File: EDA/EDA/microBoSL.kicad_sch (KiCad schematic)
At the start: 57 parts

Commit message: rebase for adding wireless to microbosl
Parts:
- removed C12, C13, C14, C2, C3, C4, C7: (no value), symbol Device:C
- removed D4: (no value), symbol Device:D
- removed J10, J9: (no value), symbol Connector_Generic:Conn_01x02
- removed J11, J12, J13, J2, J5: (no value), symbol Connector_Generic:Conn_01x03
- removed J6: (no value), symbol Connector_Generic:Conn_01x04
- removed Q1, Q2: (no value), symbol microBoSL-rescue:DMP2165UW
- removed R1, R11, R12, R5, R6: (no value), symbol Device:R
- removed SW2: (no value), symbol microBoSL-rescue:AYZ0103AGRLC
- removed U10: (no value), symbol microBoSL-rescue:TPS709A33DBVT
- removed U3: (no value), Package_DFN_QFN:QFN-28-1EP_4x4mm_P0.45mm_EP2.4x2.4mm, symbol MCU_Microchip_ATmega:ATmega328P-MM
- removed U4, U8, U9: (no value), symbol Driver_Motor:ZXBM5210-S
- removed U?: (no value), symbol Timer_RTC:MCP7940N-xSN
- added J2: (no value), symbol Connector_Generic:Conn_02x03_Odd_Even
- added J3: (no value), symbol Connector_Generic:Conn_01x04
- added J6: (no value), symbol Connector_Generic:Conn_01x10
- added Q1: (no value), symbol Device:Q_NMOS_GSD
- added R2: (no value), symbol Device:R
- added U1, U2: (no value), symbol Analog_Switch:MAX40200ANS
- added U3: (no value), symbol Regulator_Linear:MCP1700-3302E_SOT23
- added U4: (no value), symbol microBoSL-rescue:ATmega328-MMH-MCU_Microchip_ATmega
- added U5: (no value), symbol microBoSL-rescue:MCP7940N-xSN-Timer
- C1: Supplier https://au.mouser.com/ProductDetail/Samsung-Electro-Mechani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 -> (none)
- C2: renamed from C6; Supplier https://au.mouser.com/ProductDetail/KEMET/C0402C150J8HACTU?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 -> (none)
- C3: renamed from C5; Supplier https://au.mouser.com/ProductDetail/KEMET/C0402C150J8HACTU?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 -> (none)
- C4: renamed from C9; Supplier https://au.mouser.com/ProductDetail/KEMET/C0402C150J8HACTU?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 -> (none)
- C5: renamed from C8; Supplier https://au.mouser.com/ProductDetail/KEMET/C0402C150J8HACTU?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 -> (none)
- C6: renamed from C10; Supplier https://au.mouser.com/ProductDetail/AVX/04026D104KAT2A?qs=s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 -> (none)
- C7: renamed from C11; Supplier https://au.mouser.com/ProductDetail/AVX/04026D104KAT2A?qs=s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 -> (none)
- D1: renamed from D2; Supplier https://au.mouser.com/ProductDetail/Wurth-Elektronik/150060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 -> (none)
- D2: renamed from D3; Supplier https://au.mouser.com/datasheet/2/445/150060YS55040-1714218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 -> (none)
- D3: renamed from D1; Supplier https://au.mouser.com/ProductDetail/Wurth-Elektronik/150060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 -> (none)
- J8: Supplier https://au.mouser.com/ProductDetail/Molex/105133-0001?qs=nm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 -> (none)
- R1: renamed from R2; Supplier https://au.mouser.com/ProductDetail/Vishay-Dale/CRCW040210K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 -> (none)
- R3: renamed from R4; Supplier https://au.mouser.com/ProductDetail/Vishay-Dale/CRCW040210K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 -> (none)
- R4: renamed from R3; Supplier https://au.mouser.com/ProductDetail/Vishay-Dale/CRCW040210K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 -> (none)
- R5: renamed from R7; Supplier https://au.mouser.com/ProductDetail/Vishay-Dale/CRCW040210K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 -> (none)
- R6: renamed from R8; Supplier https://au.mouser.com/ProductDetail/Vishay-Dale/CRCW04023K3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 -> (none)
- R7: renamed from R9; Supplier https://au.mouser.com/ProductDetail/Vishay-Dale/CRCW04023K3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 -> (none)
- R8: renamed from R10; Supplier https://au.mouser.com/ProductDetail/Vishay-Dale/CRCW04023K3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 -> (none)
- U6: renamed from U5; Supplier https://au.mouser.com/ProductDetail/Nexperia/74HC126PW-Q100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 -> (none)
- U7: Supplier https://au.mouser.com/ProductDetail/FTDI/FT232RQ-REEL?qs=D1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 -> (none)
- Y1: Supplier https://au.mouser.com/ProductDetail/Diodes-Incorporated/F90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 -> (none)
- Y2: Supplier https://au.mouser.com/ProductDetail/IQD/LFXTAL050789Reel?qs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 -> (none)
- renumbered J3 to J4, J4 to J5
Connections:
- net VBAT is gone; now on net VPP: J4.2 (Pin_2)
- net AREF: now also U4.17 (AREF)
- net GND: now also J7.2 (Pin_2), J2.1 (Pin_1), J2.2 (Pin_2), J3.1 (Pin_1), Q1.2 (S), R2.1, U1.B2 (GND), U2.B2 (GND), U3.1 (GND), U4.18 (GND), U4.29 (GND), U4.4 (GND), U5.3 (VBAT), U5.4 (VSS)
- net Hall_WKE_S: now also J2.5 (Pin_5), U4.21 (PC2)
- net RTC_I: now also U4.28 (PD2), U5.7 (MFP)
- net SCL: now also U4.24 (PC5), U5.6 (SCL)
- net SDA: now also U4.23 (PC4), U5.5 (SDA)
- net TLL_RST: now also J3.2 (Pin_2), U4.25 (~{RESET}/PC6)
- net TLL_RX: now also J3.3 (Pin_3), U4.26 (PD0)
- net TLL_TX: now also J3.4 (Pin_4), U4.27 (PD1)
- net USB_V: now also U1.A1 (VDD), U1.B1 (EN)
- net VPP: now also U2.A1 (VDD), U2.B1 (EN)
- net V_3.3: now also U3.2 (VO), U4.16 (AVCC), U4.3 (VCC), U5.8 (VCC)
- net at C2.2, Y1.1: now also U4.6 (XTAL2/PB7)
- net at C3.2, Y1.3: now also U4.5 (XTAL1/PB6)
- net at C4.2, Y2.1: now also U5.1 (X1)
- net at C5.2, Y2.2: now also U5.2 (X2)
- net at J7.1 (Pin_1): now also Q1.3 (D)
- new net: U1.A2 (OUT), U2.A2 (OUT), U3.3 (VI)
- new net A1: J6.9 (Pin_9), U4.20 (PC1)
- new net A3: J6.10 (Pin_10), U4.22 (PC3)
- new net D10: J6.5 (Pin_5), U4.12 (PB2)
- new net D11: J6.6 (Pin_6), U4.13 (PB3)
- new net D12: J6.7 (Pin_7), U4.14 (PB4)
- new net D13: J6.8 (Pin_8), U4.15 (PB5)
- new net D3: J6.1 (Pin_1), U4.1 (PD3)
- new net D4: J6.2 (Pin_2), U4.2 (PD4)
- new net D7: J6.3 (Pin_3), U4.9 (PD7)
- new net D8: J6.4 (Pin_4), U4.10 (PB0)
- new net Hall_CNT_P: J2.4 (Pin_4), U4.8 (PD6)
- new net Hall_CNT_S: J2.6 (Pin_6), U4.19 (PC0)
- new net Hall_WKE_P: J2.3 (Pin_3), U4.7 (PD5)
- new net MOSFET: Q1.1 (G), R2.2, U4.11 (PB1)
- no-connect marks 18 -> 15
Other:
- note added: "Hall Count"
- note added: "Motor MOSFET"
- note removed: "Battery Switch"
- note removed: "Motor H Bridges"
- moved on the sheet: C2, C3, C4, C5, C6, C7, D1, D2, D3, J1, J4, J5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

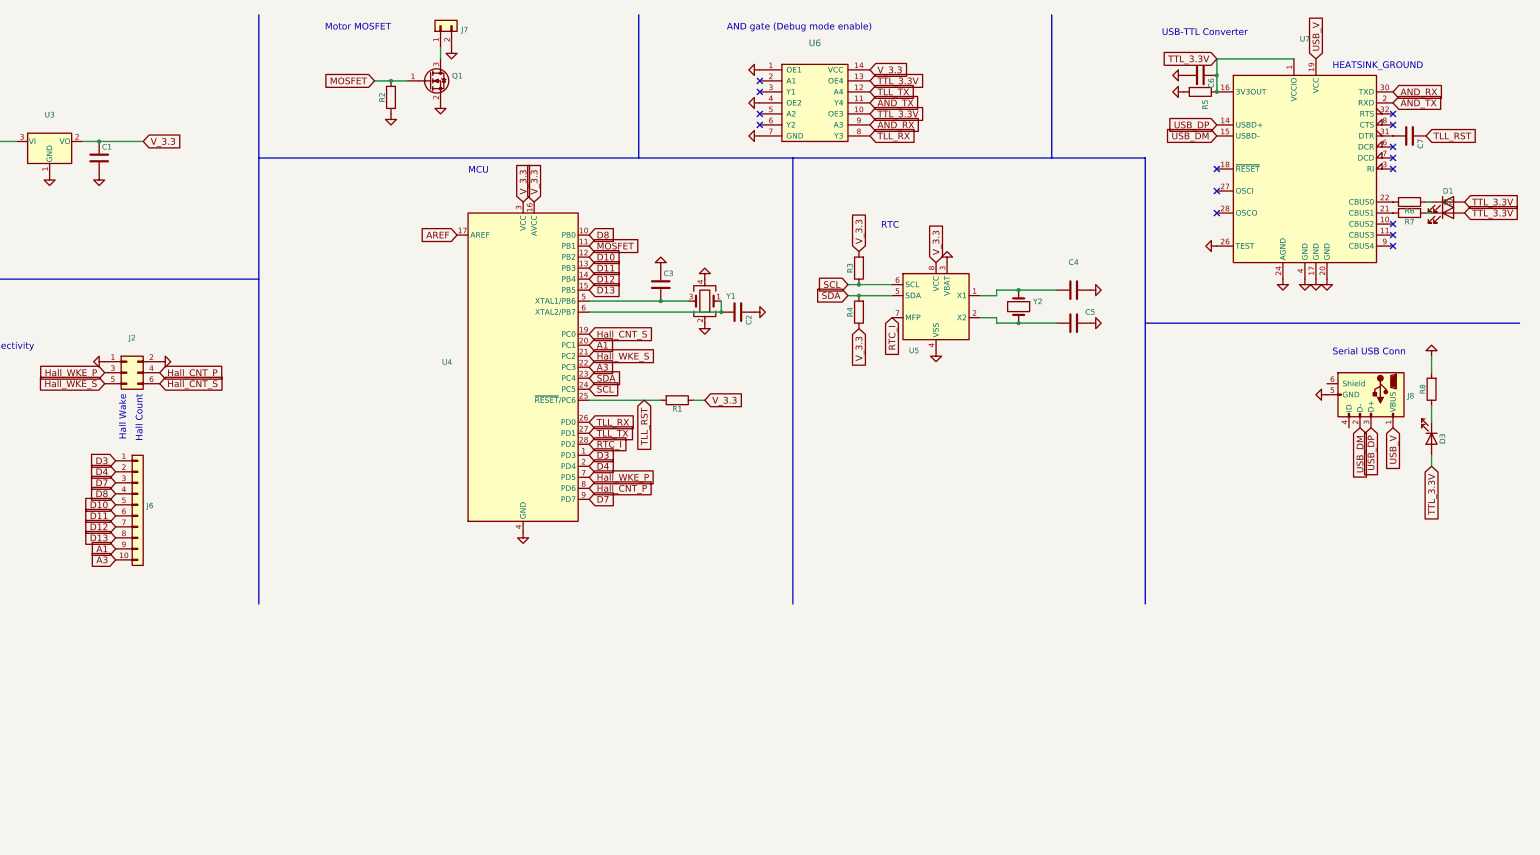
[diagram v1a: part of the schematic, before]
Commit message: added Si4463 radio module
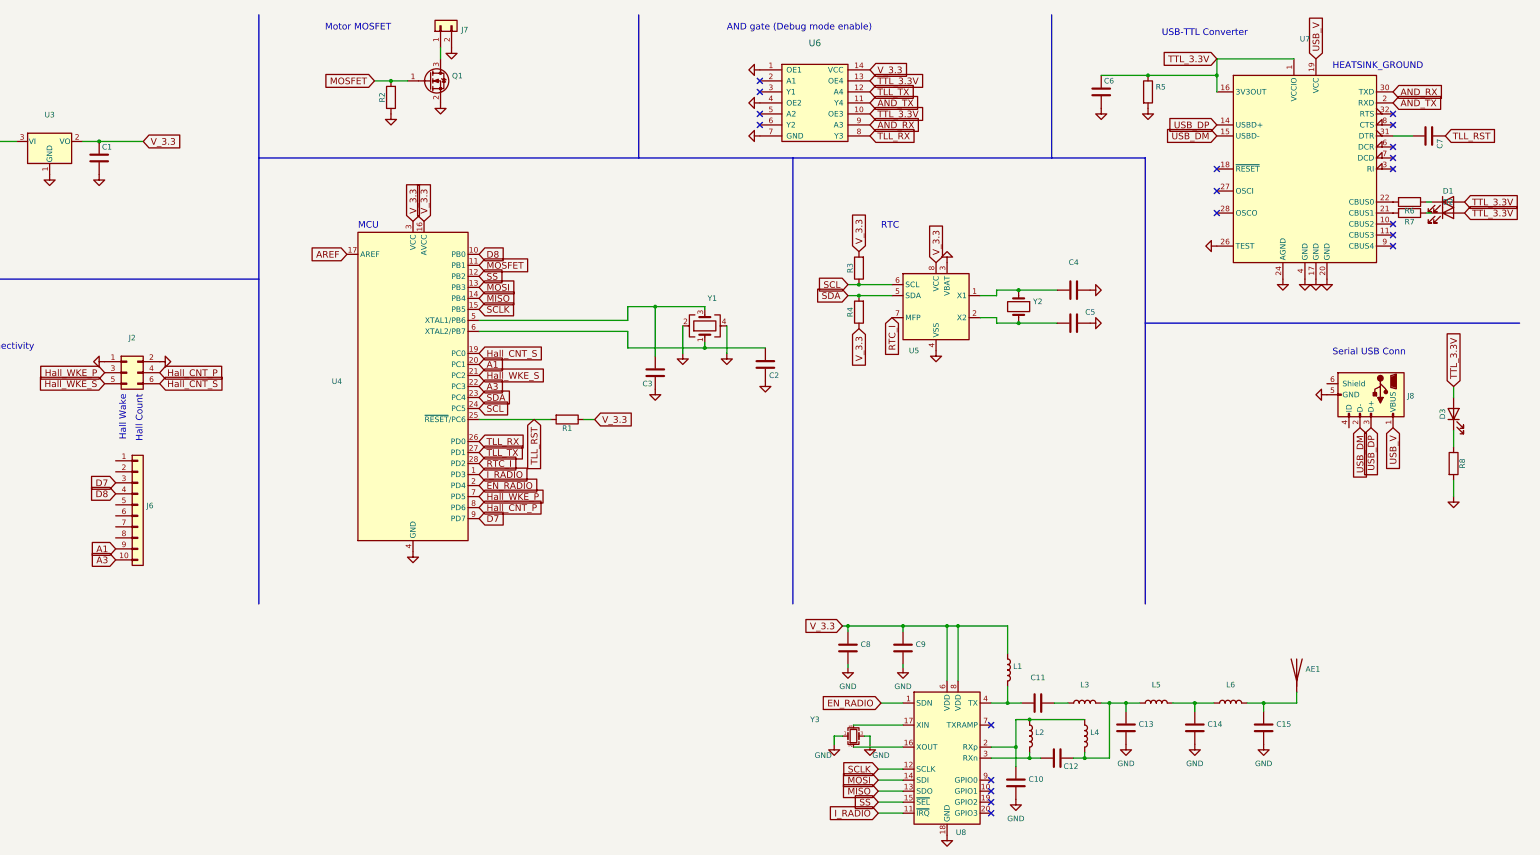
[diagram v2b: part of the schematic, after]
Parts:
- added AE1: (no value), symbol Device:Antenna
- added C10, C12, C13, C14, C15: (no value), Capacitor_SMD:C_0402_1005Metric, symbol Device:C
- added C11, C8, C9: (no value), symbol Device:C
- added L1, L2: (no value), symbol Device:L
- added L3, L4, L5, L6: (no value), Inductor_SMD:L_0402_1005Metric, symbol Device:L
- added U8: (no value), symbol RF:Si4463
- added Y3: (no value), symbol Device:Crystal_GND24_Small
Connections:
- net GND: now also C10.2, C13.2, C14.2, C15.2, C8.2, C9.2, U8.18 (GND), U8.21 (GND), Y3.1, Y3.3
- net V_3.3: now also C8.1, C9.1, L1.1, U8.6 (VDD), U8.8 (VDD)
- net D10: no longer names the net of J6.5 (Pin_5)
- net D10: no longer U4.12 (PB2)
- net D11: no longer names the net of J6.6 (Pin_6)
- net D11: no longer U4.13 (PB3)
- net D12: no longer names the net of J6.7 (Pin_7)
- net D12: no longer U4.14 (PB4)
- net D13: no longer names the net of J6.8 (Pin_8)
- net D13: no longer U4.15 (PB5)
- net D3: no longer names the net of J6.1 (Pin_1)
- net D3: no longer U4.1 (PD3)
- net D4: no longer names the net of J6.2 (Pin_2)
- net D4: no longer U4.2 (PD4)
- new net: C12.1, C13.1, L3.2, L4.2, L5.1
- new net: C14.1, L5.2, L6.1
- new net: C11.1, L3.1
- new net: C11.2, L1.2, U8.4 (TX)
- new net: C10.1, L2.1, L4.1, U8.2 (RXp)
- new net: C12.2, L2.2, U8.3 (RXn)
- new net: AE1.1 (A), C15.1, L6.2
- new net: U8.16 (XOUT), Y3.2
- new net: U8.17 (XIN), Y3.4
- new net EN_RADIO: U4.2 (PD4), U8.1 (SDN)
- new net I_RADIO: U4.1 (PD3), U8.11 (~{IRQ})
- new net MISO: U4.14 (PB4), U8.13 (SDO)
- new net MOSI: U4.13 (PB3), U8.14 (SDI)
- new net SCLK: U4.15 (PB5), U8.12 (SCLK)
- new net SS: U4.12 (PB2), U8.15 (~{SEL})
- no-connect marks 15 -> 20
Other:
- moved on the sheet: C2, C3, C6, C7, D3, R1, R5, R8, U4, Y1

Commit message: finalised schematic for radio microbosl
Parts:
- removed J2: (no value), symbol Connector_Generic:Conn_02x03_Odd_Even
- removed J6: (no value), symbol Connector_Generic:Conn_01x10
- removed J7: (no value), symbol Connector_Generic:Conn_01x02
- removed Q1: (no value), symbol Device:Q_NMOS_GSD
- removed U1, U2: (no value), symbol Analog_Switch:MAX40200ANS
- removed U3: (no value), symbol Regulator_Linear:MCP1700-3302E_SOT23
- removed U5: (no value), symbol microBoSL-rescue:MCP7940N-xSN-Timer
- added C16: 100 nF, Capacitor_SMD:C_0402_1005Metric, symbol Device:C
- added C17, C18: 15 pF, Capacitor_SMD:C_0402_1005Metric, symbol Device:C
- added D4: CUS08F30,H3F, Diode_SMD:D_SOD-323, symbol Device:D
- added F1: (no value), symbol Device:Fuse_Small
- added J2: Conn_01x03, Connector_PinHeader_2.54mm:PinHeader_1x03_P2.54mm_Vertical, symbol Connector_Generic:Conn_01x03
- added J6, J7: (no value), symbol Connector_Generic:Conn_01x03
- added J9: MOTOR_OUT, Connector_PinHeader_2.54mm:PinHeader_1x02_P2.54mm_Vertical, symbol Connector_Generic:Conn_01x02
- added Q1, Q2: DMP2165UW, Package_TO_SOT_SMD:SOT-323_SC-70, symbol microBoSL-rescue:DMP2165UW
- added R10, R9: 10 kΩ, Resistor_SMD:R_0402_1005Metric, symbol Device:R
- added R11, R12: 4.7 MΩ, Capacitor_SMD:C_0402_1005Metric, symbol Device:R
- added SW2: (no value), symbol Switch:SW_SPDT
- added U1: TPS709A33DBVT, Package_TO_SOT_SMD:SOT-23-5, symbol microBoSL-rescue:TPS709A33DBVT
- added U2: ZXBM5210-S, Package_SO:SOIC-8_3.9x4.9mm_P1.27mm, symbol Driver_Motor:ZXBM5210-S
- added U3: (no value), symbol Timer_RTC:MCP7940N-xMNY
- AE1: value (none) -> Antenna; footprint (none) -> Connector_PinHeader_2.54mm:PinHeader_1x01_P2.54mm_Vertical
- C1: value (none) -> 2.2 μF; footprint (none) -> Capacitor_SMD:C_0805_2012Metric; Supplier (none) -> https://au.mouser.com/ProductDetail/Samsung-Electro-Mechani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
- C10, C12: value (none) -> 5.1 pF
- C11: value (none) -> 6.8 pF; footprint (none) -> Capacitor_SMD:C_0402_1005Metric
- C13: value (none) -> 12 pF
- C14: value (none) -> 18 pF
- C15: value (none) -> 9.1 pF
- C2, C3: value (none) -> 22 pF; footprint (none) -> Capacitor_SMD:C_0402_1005Metric
- C4, C5: value (none) -> 100 nF; footprint (none) -> Capacitor_SMD:C_0402_1005Metric; Supplier (none) -> https://au.mouser.com/ProductDetail/AVX/04026D104KAT2A?qs=s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
- C6, C7: value (none) -> 100 nF; footprint (none) -> Capacitor_SMD:C_0603_1608Metric
- C8: value (none) -> 100 pF; footprint (none) -> Capacitor_SMD:C_0402_1005Metric
- C9: value (none) -> 100 nF; footprint (none) -> Capacitor_SMD:C_0402_1005Metric
- D1, D2, D3: value (none) -> LED; footprint (none) -> LED_SMD:LED_0603_1608Metric
- J1, J4: value (none) -> Conn_01x04; footprint (none) -> Connector_PinHeader_2.54mm:PinHeader_1x04_P2.54mm_Vertical
- J3: value (none) -> Conn_01x04; footprint (none) -> Connector_PinHeader_1.27mm:PinHeader_1x04_P1.27mm_Vertical
- J5: value (none) -> Conn_01x02; footprint (none) -> Connector_PinHeader_2.54mm:PinHeader_1x02_P2.54mm_Vertical
- J8: value (none) -> USB_B_Micro; footprint (none) -> Connector_USB:USB_Micro-B_Molex-105133-0001
- L1: value (none) -> 220 nH; footprint (none) -> Inductor_SMD:L_0402_1005Metric
- L2: value (none) -> 68 nH; footprint (none) -> Inductor_SMD:L_0402_1005Metric
- L3: value (none) -> 24 nH
- L4: value (none) -> 27 nH
- L5, L6: value (none) -> 12 nH
- R1, R5: value (none) -> 10 kΩ; footprint (none) -> Resistor_SMD:R_0402_1005Metric
- R2, R3: value (none) -> 10 kΩ; footprint (none) -> Resistor_SMD:R_0402_1005Metric; Supplier (none) -> https://au.mouser.com/ProductDetail/Vishay-Dale/CRCW040210K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
- R4: value (none) -> 4.7 MΩ; footprint (none) -> Capacitor_SMD:C_0402_1005Metric; Supplier (none) -> https://au.mouser.com/ProductDetail/Vishay-Dale/CRCW04024M7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
- R6, R7, R8: value (none) -> 3.3 kΩ; footprint (none) -> Resistor_SMD:R_0402_1005Metric
- U4: value (none) -> ATmega328-MMH; footprint (none) -> Package_DFN_QFN:QFN-28-1EP_4x4mm_P0.45mm_EP2.4x2.4mm
- U6: value (none) -> 74HC126PW-Q100; footprint (none) -> Package_SO:TSSOP-14_4.4x5mm_P0.65mm
- U7: value (none) -> FT232RQ; footprint (none) -> Package_DFN_QFN:QFN-32-1EP_5x5mm_P0.5mm_EP3.1x3.1mm
- U8: value (none) -> Si4463; footprint (none) -> Package_DFN_QFN:QFN-20-1EP_4x4mm_P0.5mm_EP2.6x2.6mm_ThermalVias
- Y1: value (none) -> 8MHz; footprint (none) -> Crystal:Crystal_SMD_EuroQuartz_MT-4Pin_3.2x2.5mm
- Y2: value (none) -> 32.768 kHz; footprint (none) -> Crystal:Crystal_SMD_2012-2Pin_2.0x1.2mm; Supplier (none) -> https://au.mouser.com/ProductDetail/IQD/LFXTAL050789Reel?qs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
- Y3: value (none) -> 30 MHz; footprint (none) -> Crystal:Crystal_SMD_Abracon_ABM8G-4Pin_3.2x2.5mm
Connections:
- net A1: now also J2.2 (Pin_2)
- net A3: now also J2.3 (Pin_3)
- net D7: now also J2.1 (Pin_1)
- net GND: now also C5.2, R4.1, C16.2, C17.1, C18.1, J6.2 (Pin_2), J7.2 (Pin_2), R12.2, SW2.1 (A), U1.2 (GND), U2.8 (GND), U3.4 (VSS), U3.9 (EP); no longer C5.1, R2.1
- net Hall_CNT_P: now also J6.3 (Pin_3)
- net Hall_CNT_S: now also J6.1 (Pin_1)
- net Hall_WKE_P: now also J7.3 (Pin_3)
- net Hall_WKE_S: now also J7.1 (Pin_1)
- net RTC_I: now also U3.7 (MFP)
- net SCL: now also R10.1, U3.6 (SCL); no longer R3.1
- net SDA: now also R9.2, U3.5 (SDA); no longer R4.2
- net USB_V: now also R2.2, D4.2 (A)
- net VPP: now also R3.2, F1.1, Q2.2 (S), R11.1; no longer J5.2 (Pin_2)
- net V_3.3: now also C4.2, R10.2, R9.1, U1.1 (OUT), U2.3 (VDD), U2.6 (VREF), U3.8 (VCC); no longer R3.2, R4.1
- net at Y2.1: now also C18.2, U3.1 (X1); no longer C4.2
- net at Y2.2: now also C17.2, U3.2 (X2); no longer C5.2
- net D8 renamed MREV
- net MREV: now also U2.5 (REV)
- net MOSFET renamed MFWD
- net MFWD: now also U2.4 (FWD); no longer R2.2
- new net: F1.2, J5.2 (Pin_2)
- new net: Q1.1 (G), R2.1, R4.2
- new net: D4.1 (K), Q1.2 (S), U1.3 (IN)
- new net: C16.1, R11.2, R12.1, U3.3 (VBAT)
- new net: J9.1 (Pin_1), U2.1 (OUT1)
- new net: J9.2 (Pin_2), U2.7 (OUT2)
- new net: R3.1, SW2.3 (C)
- new net: Q2.1 (G), SW2.2 (B)
- new net VBAT: C5.1, Q1.3 (D), Q2.3 (D), U2.2 (VM)
- no-connect marks 20 -> 21
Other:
- note added: "Battery Switch"
- note removed: "Motor MOSFET"
- note removed: "RTC"
- moved on the sheet: J1, J3, J4, J5, SW1
